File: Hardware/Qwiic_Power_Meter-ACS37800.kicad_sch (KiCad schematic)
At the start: 31 parts, among them J1 Conn_01x01, J10 Conn_01x01, J11 Conn_01x01, J2 Conn_01x04, J3 Qwiic_RA, J4 Conn_01x01, J5 Conn_01x01, J6 Conn_01x01, J7 Qwiic_RA, J8 Conn_01x01, J9 Conn_01x01, U1 ACS37800

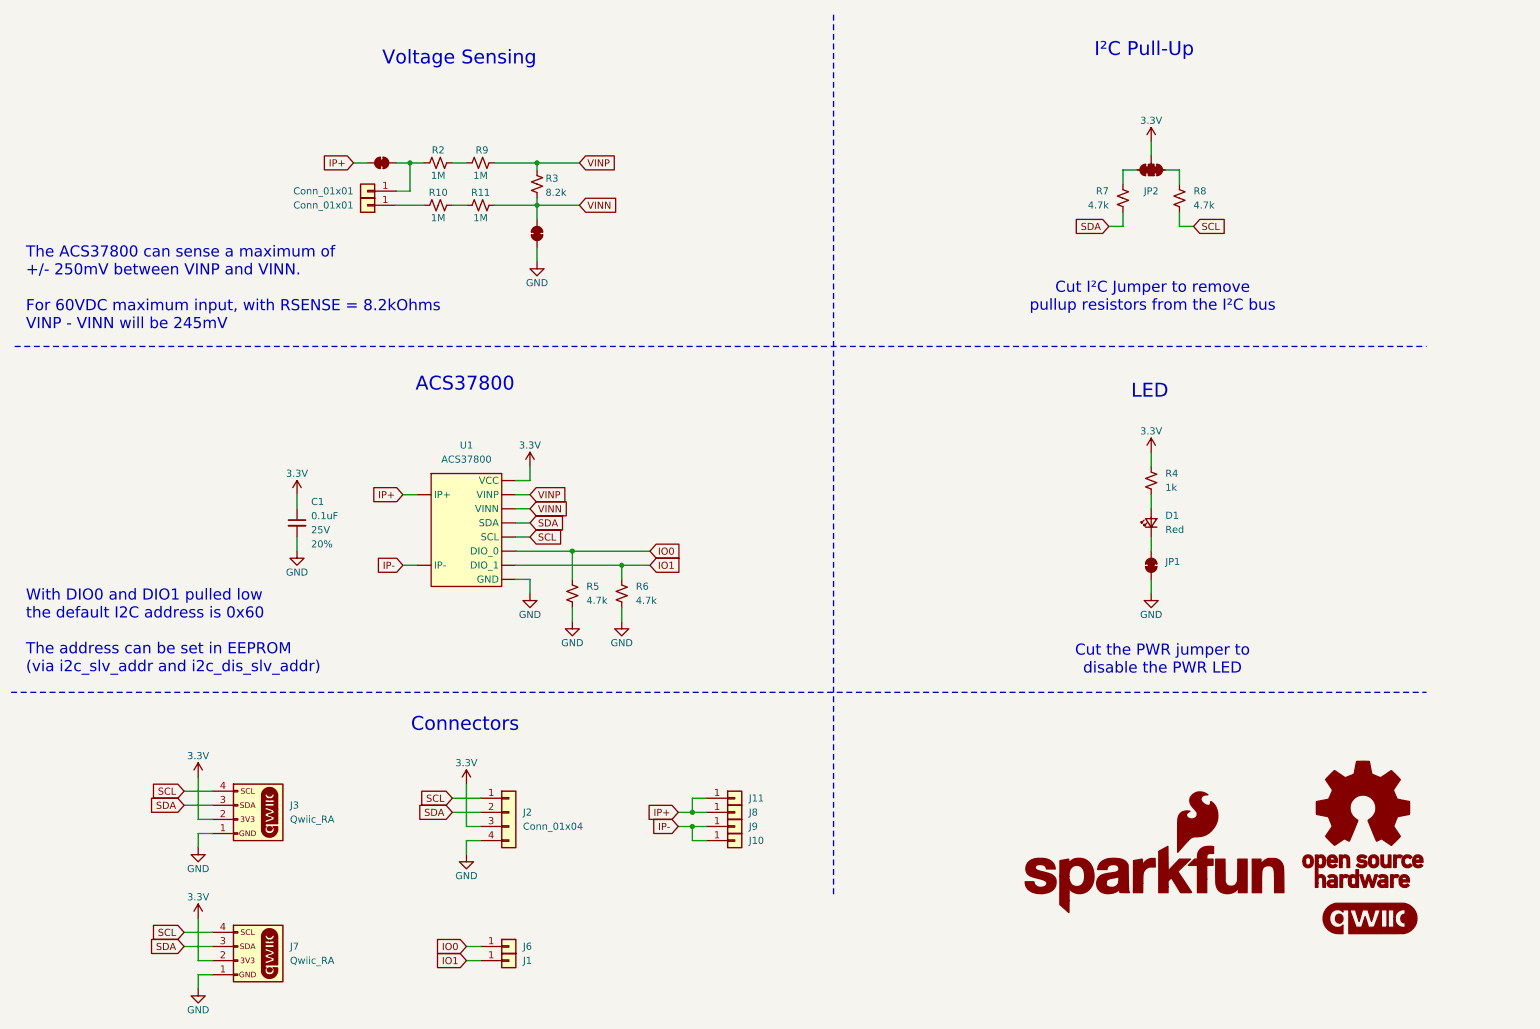
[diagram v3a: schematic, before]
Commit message: Adds measures, labels LED jumper, updates some schematic text
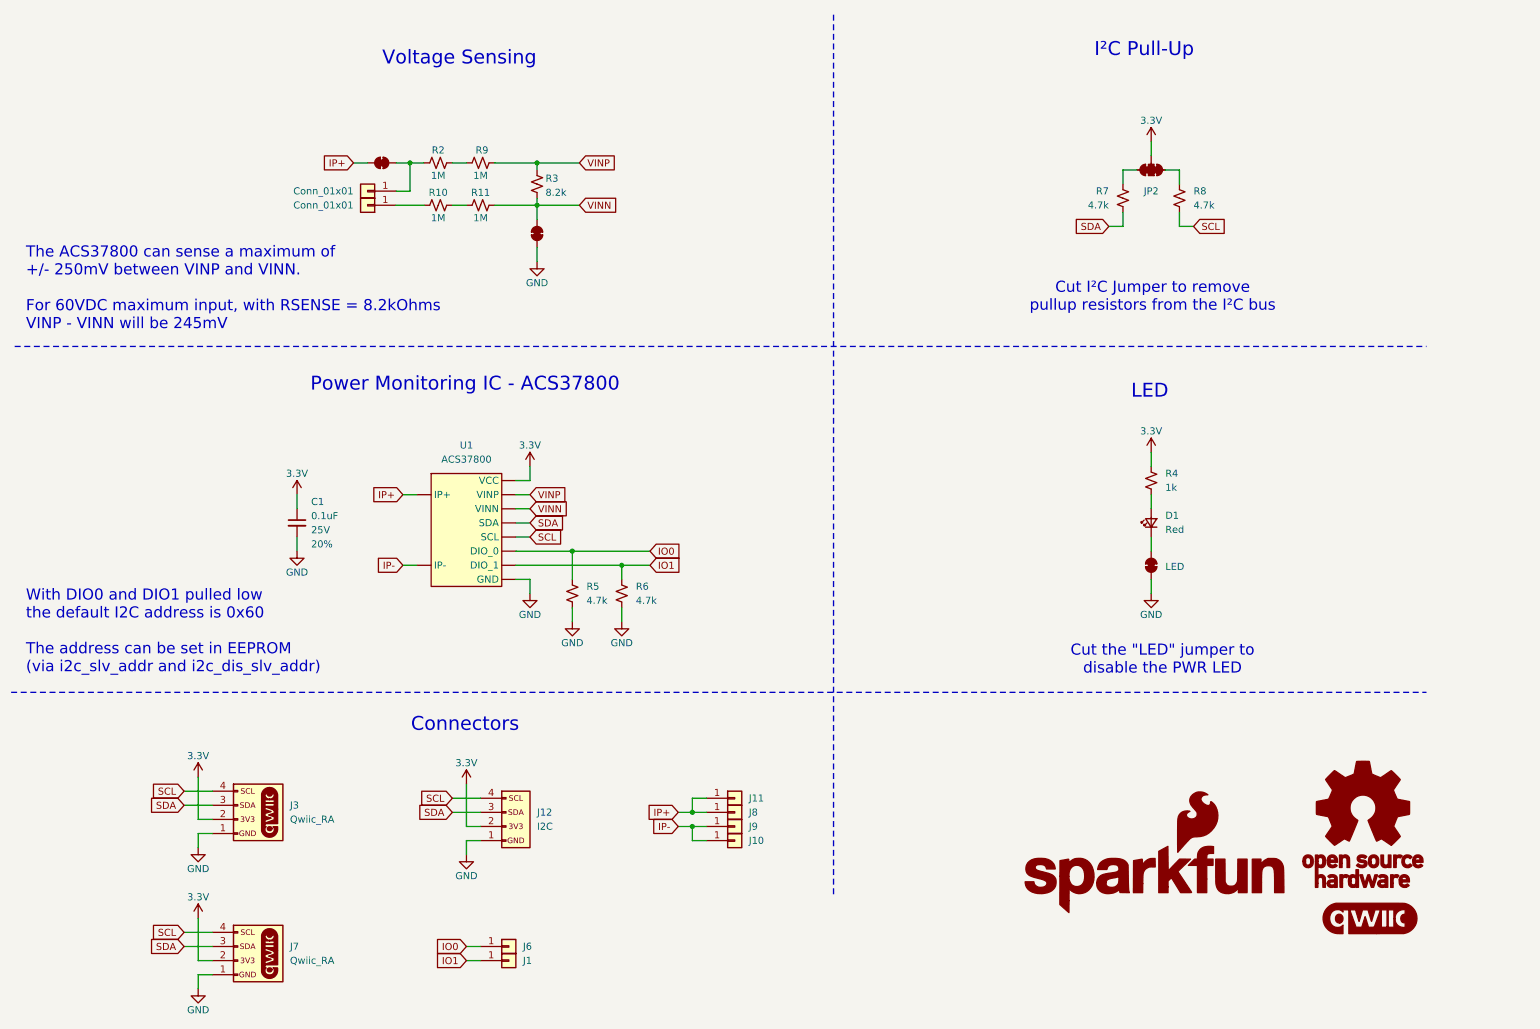
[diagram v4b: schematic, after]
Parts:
- removed J2: Conn_01x04, SparkFun-Connector:1x04, symbol SparkFun-Connector:Conn_01x04
- added J12: I2C, SparkFun-Connector:1x04, symbol SparkFun-Connector:I2C_01x04
- renumbered JP1 to LED
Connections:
- net 3.3V: now also J12.2 (Pin_2)
- net GND: now also J12.1 (Pin_1)
- net SCL: now also J12.4 (Pin_4)
- net SDA: now also J12.3 (Pin_3)
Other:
- note added: "Cut the "LED" jumper to disable the PWR LED"
- note added: "Power Monitoring IC - ACS37800"
- note removed: "ACS37800"
- note removed: "Cut the PWR jumper to disable the PWR LED"
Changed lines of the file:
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@@
 		)
 	)
-	(text "Cut the PWR jumper to\ndisable the PWR LED"
+	(text "Cut the \"LED\" jumper to\ndisable the PWR LED"
 		(exclude_from_sim no)
 		(at 219.202 128.778 0)
@@
 		)
 	)
-	(text "ACS37800"
+	(text "Power Monitoring IC - ACS37800"
 		(exclude_from_sim no)
 		(at 93.726 79.248 0)
@@
 	)
 	(symbol
-		(lib_id "SparkFun-Connector:Conn_01x04")
-		(at 101.6 156.21 0)
-		(unit 1)
-		(exclude_from_sim no)
-		(in_bom yes)
-		(on_board yes)
-		(dnp no)
-		(fields_autoplaced yes)
-		(property "Reference" "J2"
-			(at 104.14 156.2099 0)
-			(effects
-				(font
-					(size 1.27 1.27)
-				)
-				(justify left)
-			)
-		)
-		(property "Value" "Conn_01x04"
-			(at 104.14 158.7499 0)
-			(effects
-				(font
-					(size 1.27 1.27)
-				)
-				(justify left)
-			)
-		)
-		(property "Footprint" "SparkFun-Connector:1x04"
-			(at 101.6 166.37 0)
-			(effects
-				(font
-					(size 1.27 1.27)
-				)
-				(hide yes)
-			)
-		)
-		(property "Datasheet" "~"
-			(at 101.6 168.91 0)
-			(effects
-				(font
-					(size 1.27 1.27)
-				)
-				(hide yes)
-			)
-		)
-		(property "Description" "Basic 0.1\" PTH"
-			(at 101.6 171.45 0)
-			(effects
-				(font
-					(size 1.27 1.27)
-				)
-				(hide yes)
-			)
-		)
-		(pin "1"
-		)
-		(pin "2"
-		)
-		(pin "3"
-		)
-		(pin "4"
-		)
-		(instances
-			(project "Qwiic_Power_Meter-ACS37800"
-				(path "/0f119e45-4347-4dd0-98e1-ad61d69534b1"
-					(reference "J2")
-					(unit 1)
-				)
-			)
-		)
-	)
-	(symbol
 		(lib_id "SparkFun-LED:LED_Red_0603")
 		(at 217.17 104.14 90)
@@
 		(on_board yes)
 		(dnp no)
-		(fields_autoplaced yes)
-		(property "Reference" "JP1"
-			(at 219.71 111.1249 90)
+		(property "Reference" "LED"
+			(at 219.71 112.014 90)
 			(effects
 				(font
@@
 			(project "Qwiic_Power_Meter-ACS37800"
 				(path "/0f119e45-4347-4dd0-98e1-ad61d69534b1"
-					(reference "JP1")
+					(reference "LED")
 					(unit 1)
 				)
@@
 					(unit 1)
 				)
+			)
+		)
+	)
+	(symbol
+		(lib_id "SparkFun-Connector:I2C_01x04")
+		(at 101.6 156.21 0)
+		(unit 1)
+		(exclude_from_sim no)
+		(in_bom yes)
+		(on_board yes)
+		(dnp no)
+		(fields_autoplaced yes)
+		(property "Reference" "J12"
+			(at 106.68 156.2099 0)
+			(effects
+				(font
+					(size 1.27 1.27)
+				)
+				(justify left)
+			)
+		)
+		(property "Value" "I2C"
+			(at 106.68 158.7499 0)
+			(effects
+				(font
+					(size 1.27 1.27)
+				)
+				(justify left)
+			)
+		)
+		(property "Footprint" "SparkFun-Connector:1x04"
+			(at 101.6 167.64 0)
+			(effects
+				(font
+					(size 1.27 1.27)
+				)
+				(hide yes)
+			)
+		)
+		(property "Datasheet" "~"
+			(at 101.6 172.72 0)
+			(effects
+				(font
+					(size 1.27 1.27)
+				)
+				(hide yes)
+			)
+		)
+		(property "Description" "Coomon 4 pin PTH connector for I2C"
+			(at 101.6 170.18 0)
+			(effects
+				(font
+					(size 1.27 1.27)
+				)
+				(hide yes)
+			)
+		)
+		(pin "4"
+		)
+		(pin "3"
+		)
+		(pin "1"
+		)
+		(pin "2"
+		)
+		(instances
+			(project ""
+				(path "/0f119e45-4347-4dd0-98e1-ad61d69534b1"
+					(reference "J12")
+					(unit 1)
+				)

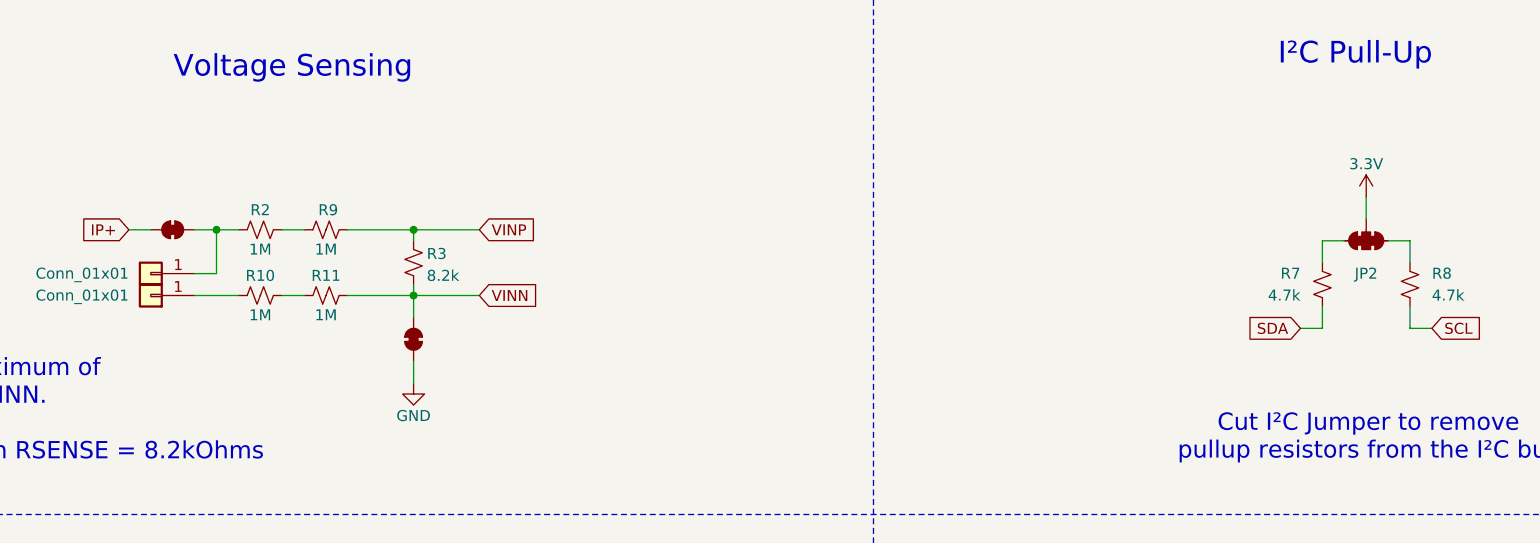
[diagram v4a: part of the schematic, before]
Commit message: Makes design 2-layer, updates jumper names in schematic
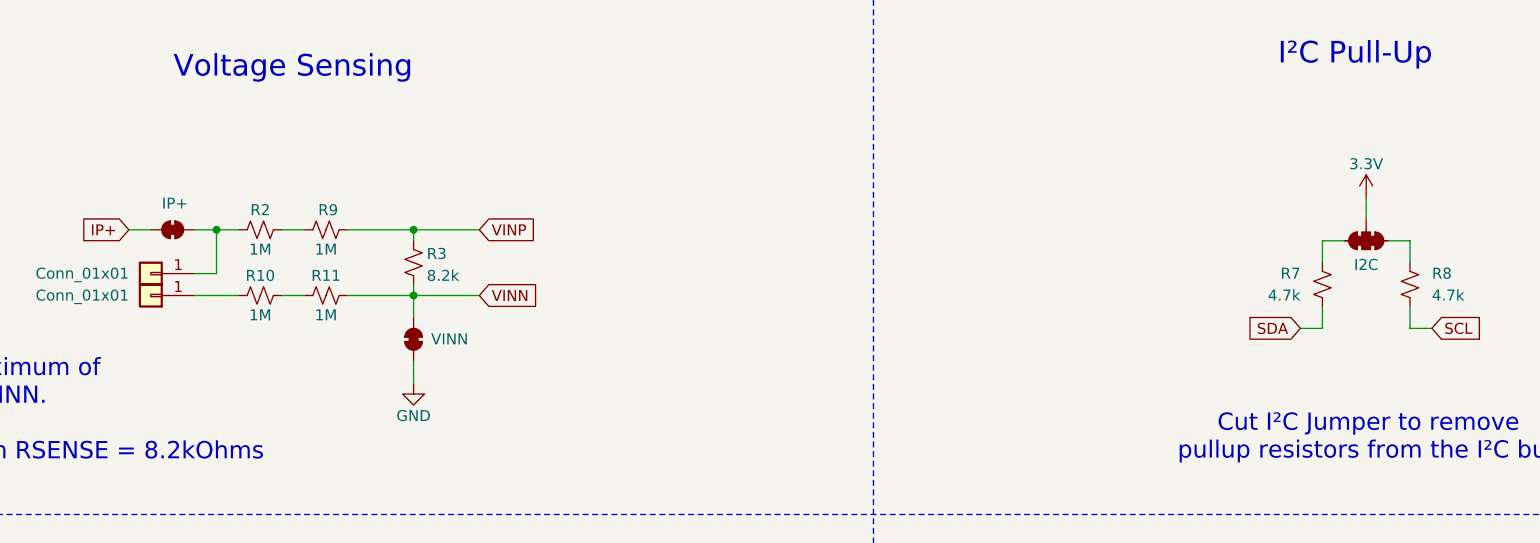
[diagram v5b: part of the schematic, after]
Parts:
- renumbered JP2 to I2C, JP3 to IP+, JP4 to VINN
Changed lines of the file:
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@@
 		(on_board yes)
 		(dnp no)
-		(fields_autoplaced yes)
-		(property "Reference" "JP2"
-			(at 217.17 44.45 0)
+		(property "Reference" "I2C"
+			(at 217.17 43.434 0)
 			(effects
 				(font
@@
 			(project "Qwiic_Power_Meter-ACS37800"
 				(path "/0f119e45-4347-4dd0-98e1-ad61d69534b1"
-					(reference "JP2")
+					(reference "I2C")
 					(unit 1)
 				)
@@
 		(on_board yes)
 		(dnp no)
-		(property "Reference" "JP4"
-			(at 109.22 51.4349 90)
+		(property "Reference" "VINN"
+			(at 108.712 52.07 90)
 			(effects
 				(font
@@
 				)
 				(justify left)
-				(hide yes)
 			)
 		)
@@
 			(project "Qwiic_Power_Meter-ACS37800"
 				(path "/0f119e45-4347-4dd0-98e1-ad61d69534b1"
-					(reference "JP4")
+					(reference "VINN")
 					(unit 1)
 				)
@@
 		(on_board yes)
 		(dnp no)
-		(fields_autoplaced yes)
-		(property "Reference" "JP3"
-			(at 78.74 34.29 0)
-			(effects
-				(font
-					(size 1.27 1.27)
-				)
-				(hide yes)
+		(property "Reference" "IP+"
+			(at 78.994 36.322 0)
+			(effects
+				(font
+					(size 1.27 1.27)
+				)
 			)
 		)
@@
 			(project "Qwiic_Power_Meter-ACS37800"
 				(path "/0f119e45-4347-4dd0-98e1-ad61d69534b1"
-					(reference "JP3")
-					(unit 1)
-				)
+					(reference "IP+")
+					(unit 1)
+				)

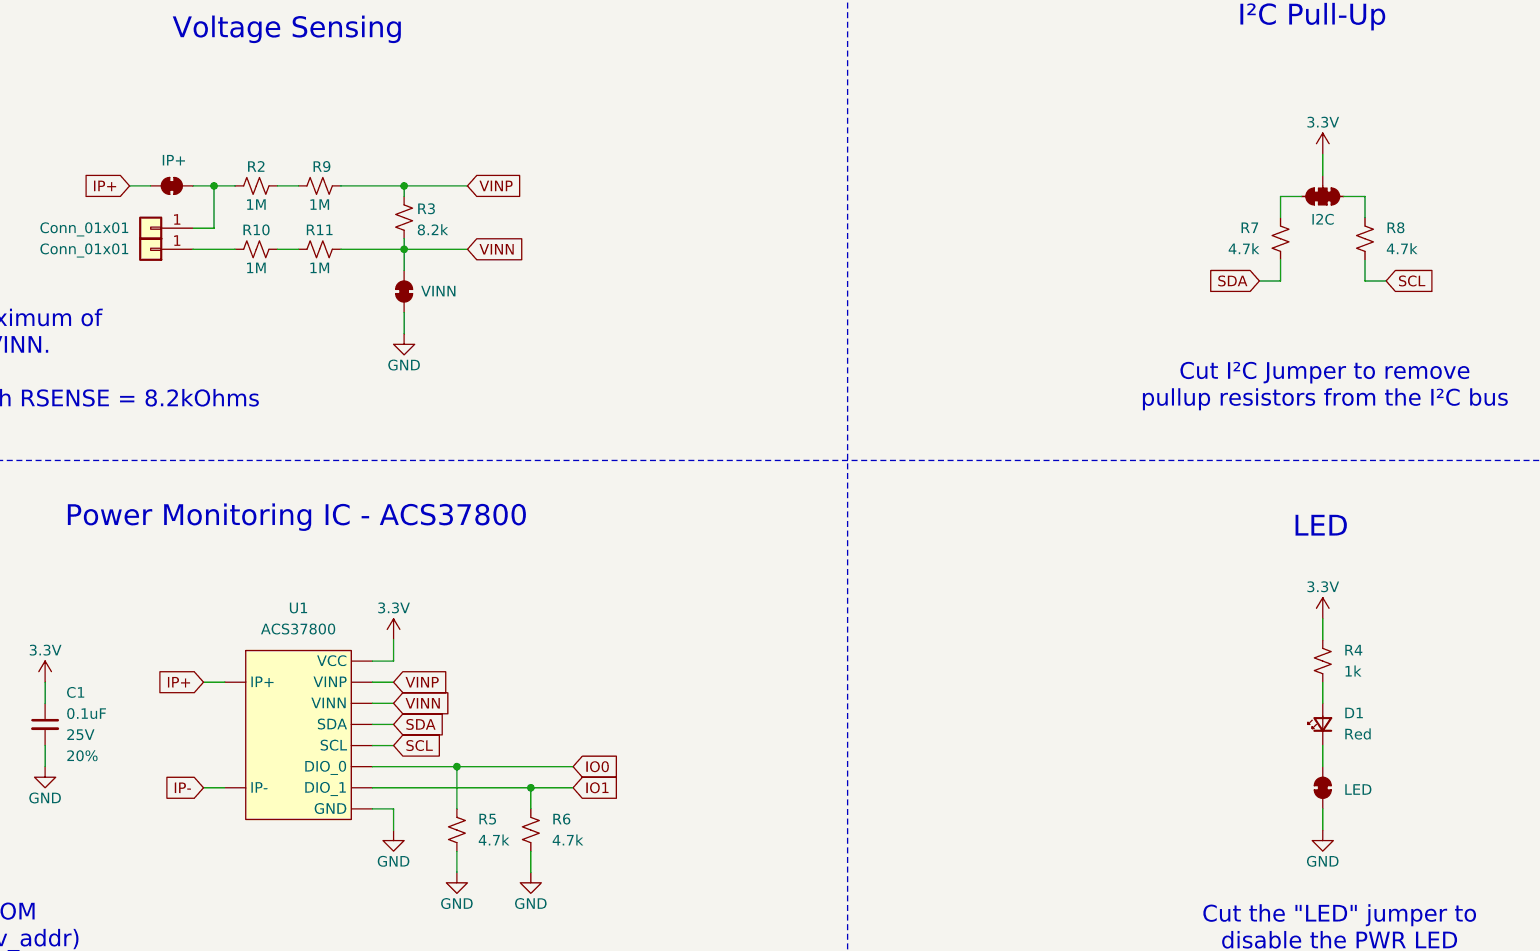
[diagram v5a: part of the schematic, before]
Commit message: Fixes some missing traces
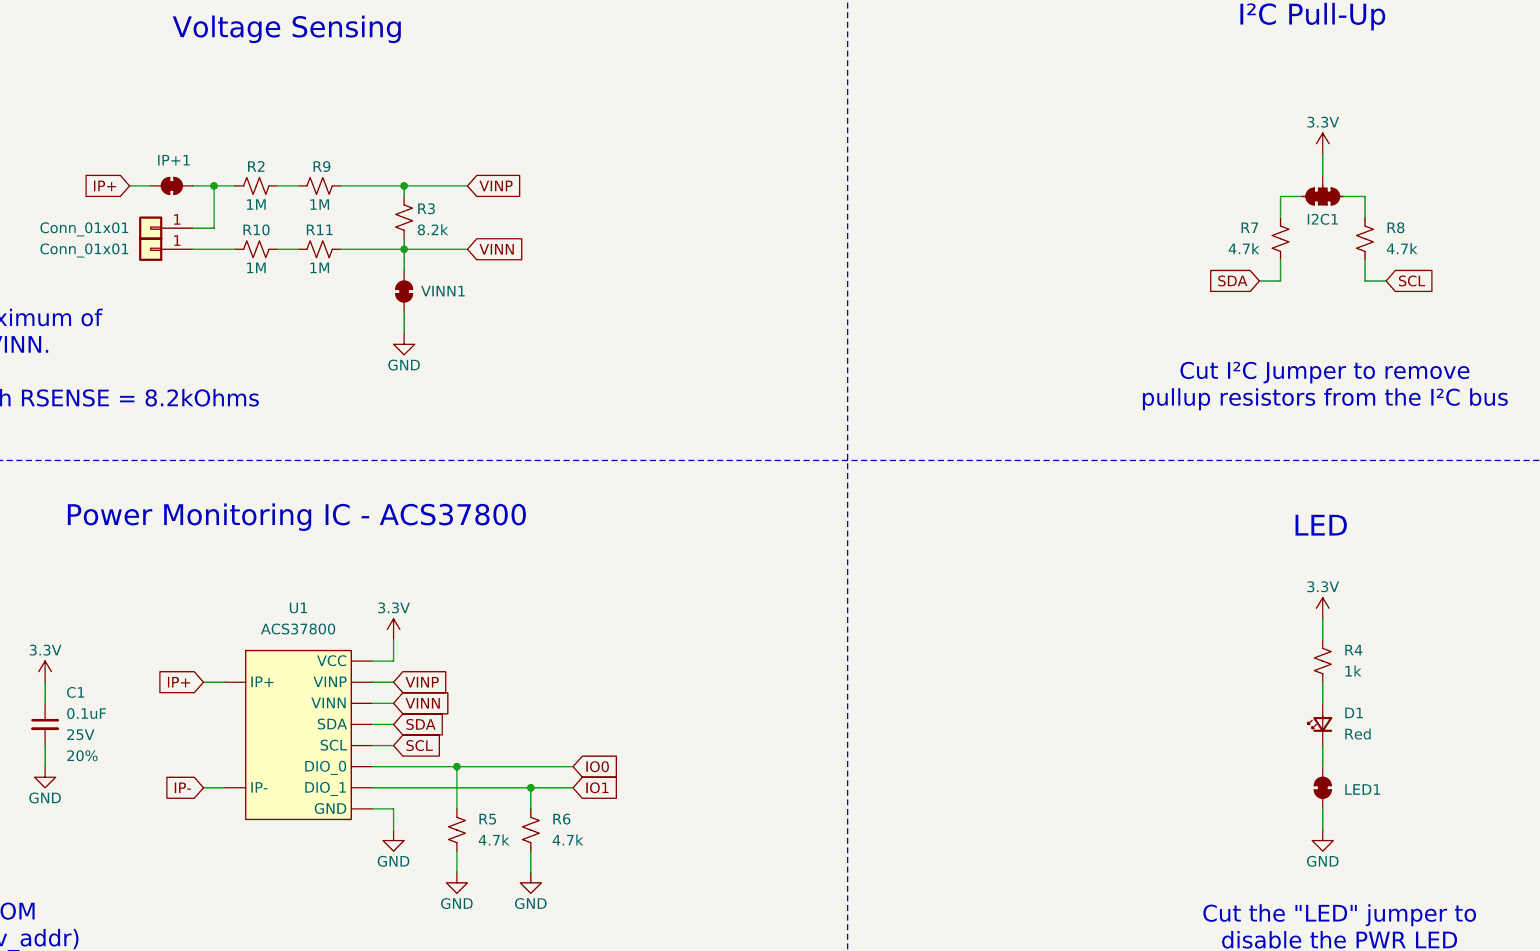
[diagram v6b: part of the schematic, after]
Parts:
- renumbered I2C to I2C1, IP+ to IP+1, LED to LED1, VINN to VINN1
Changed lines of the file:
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@@
 		(on_board yes)
 		(dnp no)
-		(property "Reference" "I2C"
+		(property "Reference" "I2C1"
 			(at 217.17 43.434 0)
 			(effects
@@
 			(project "Qwiic_Power_Meter-ACS37800"
 				(path "/0f119e45-4347-4dd0-98e1-ad61d69534b1"
-					(reference "I2C")
+					(reference "I2C1")
 					(unit 1)
 				)
@@
 		(on_board yes)
 		(dnp no)
-		(property "Reference" "VINN"
+		(property "Reference" "VINN1"
 			(at 108.712 52.07 90)
 			(effects
@@
 			(project "Qwiic_Power_Meter-ACS37800"
 				(path "/0f119e45-4347-4dd0-98e1-ad61d69534b1"
-					(reference "VINN")
+					(reference "VINN1")
 					(unit 1)
 				)
@@
 		(on_board yes)
 		(dnp no)
-		(property "Reference" "IP+"
+		(property "Reference" "IP+1"
 			(at 78.994 36.322 0)
 			(effects
@@
 			(project "Qwiic_Power_Meter-ACS37800"
 				(path "/0f119e45-4347-4dd0-98e1-ad61d69534b1"
-					(reference "IP+")
+					(reference "IP+1")
 					(unit 1)
 				)
@@
 		(on_board yes)
 		(dnp no)
-		(property "Reference" "LED"
+		(property "Reference" "LED1"
 			(at 219.71 112.014 90)
 			(effects
@@
 			(project "Qwiic_Power_Meter-ACS37800"
 				(path "/0f119e45-4347-4dd0-98e1-ad61d69534b1"
-					(reference "LED")
-					(unit 1)
-				)
+					(reference "LED1")
+					(unit 1)
+				)

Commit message: Adds some more notes to the design
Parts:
- JP1: renamed from LED1; value ~ -> LED
- JP2: renamed from I2C1; value ~ -> I2C
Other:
- note added: "Default 7-bit unshifted I^{2}C Addres: 0x60"
- note added: "I2C address can be changed in EEPROM"
- note removed: "With DIO0 and DIO1 pulled low the default I2C address is 0x60 The address can be set in EEPROM (via i2c_slv_addr and i2c_dis_slv_addr)"
- moved on the sheet: C1, IP+1, R10, R11, R2, R3, R5, R6, R9, U1, VINN1
